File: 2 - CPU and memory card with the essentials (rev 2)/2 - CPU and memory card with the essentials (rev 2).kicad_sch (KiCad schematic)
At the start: 7 parts, among them J1 BUS 1, U1 74HC74, X1 20 MHz, X2 3.6864 MHz

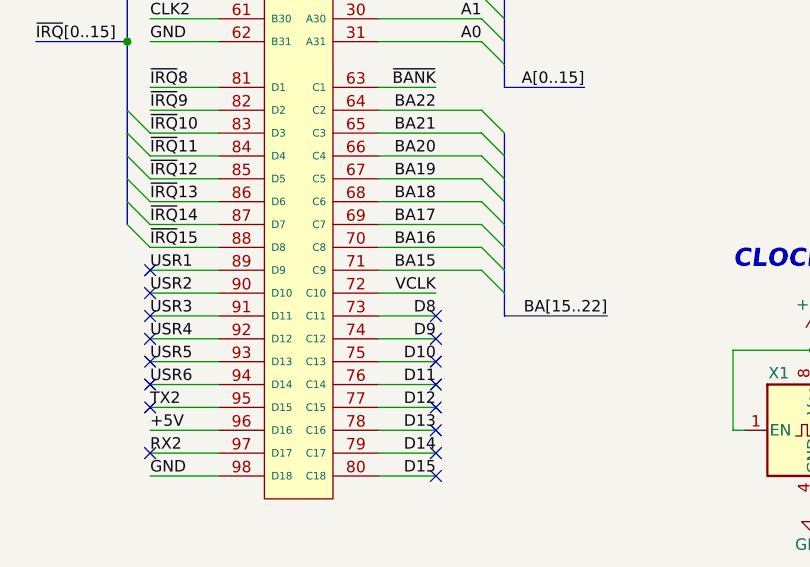
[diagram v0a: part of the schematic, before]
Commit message: Minor tweaks to the backplane, and will be sending it out for manufacture
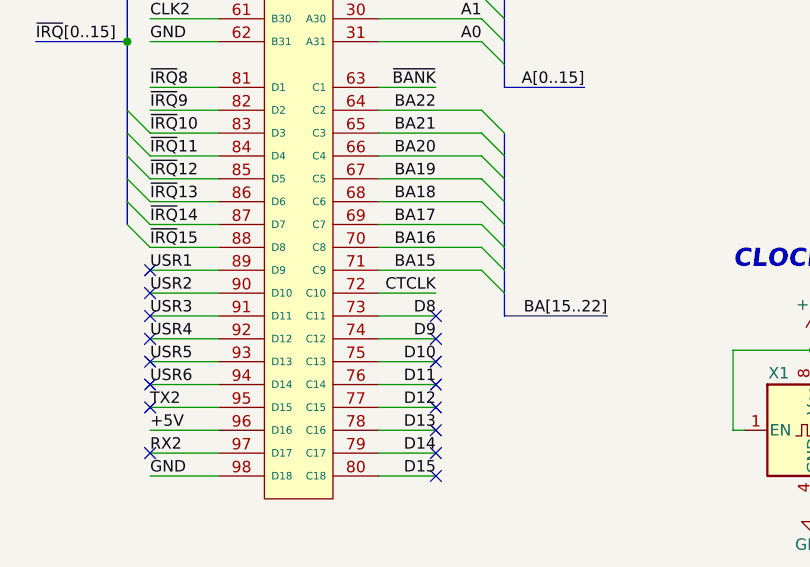
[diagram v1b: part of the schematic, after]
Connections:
- net VCLK: no longer J1.72 (C10)
- new net CTCLK: J1.72 (C10)
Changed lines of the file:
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@@
     (effects (font (size 1.27 1.27)) (justify left bottom))
   )
-  (label "VCLK" (at 59.69 129.54 180) (fields_autoplaced)
+  (label "CTCLK" (at 59.69 129.54 180) (fields_autoplaced)
     (effects (font (size 1.27 1.27)) (justify right bottom))
   )

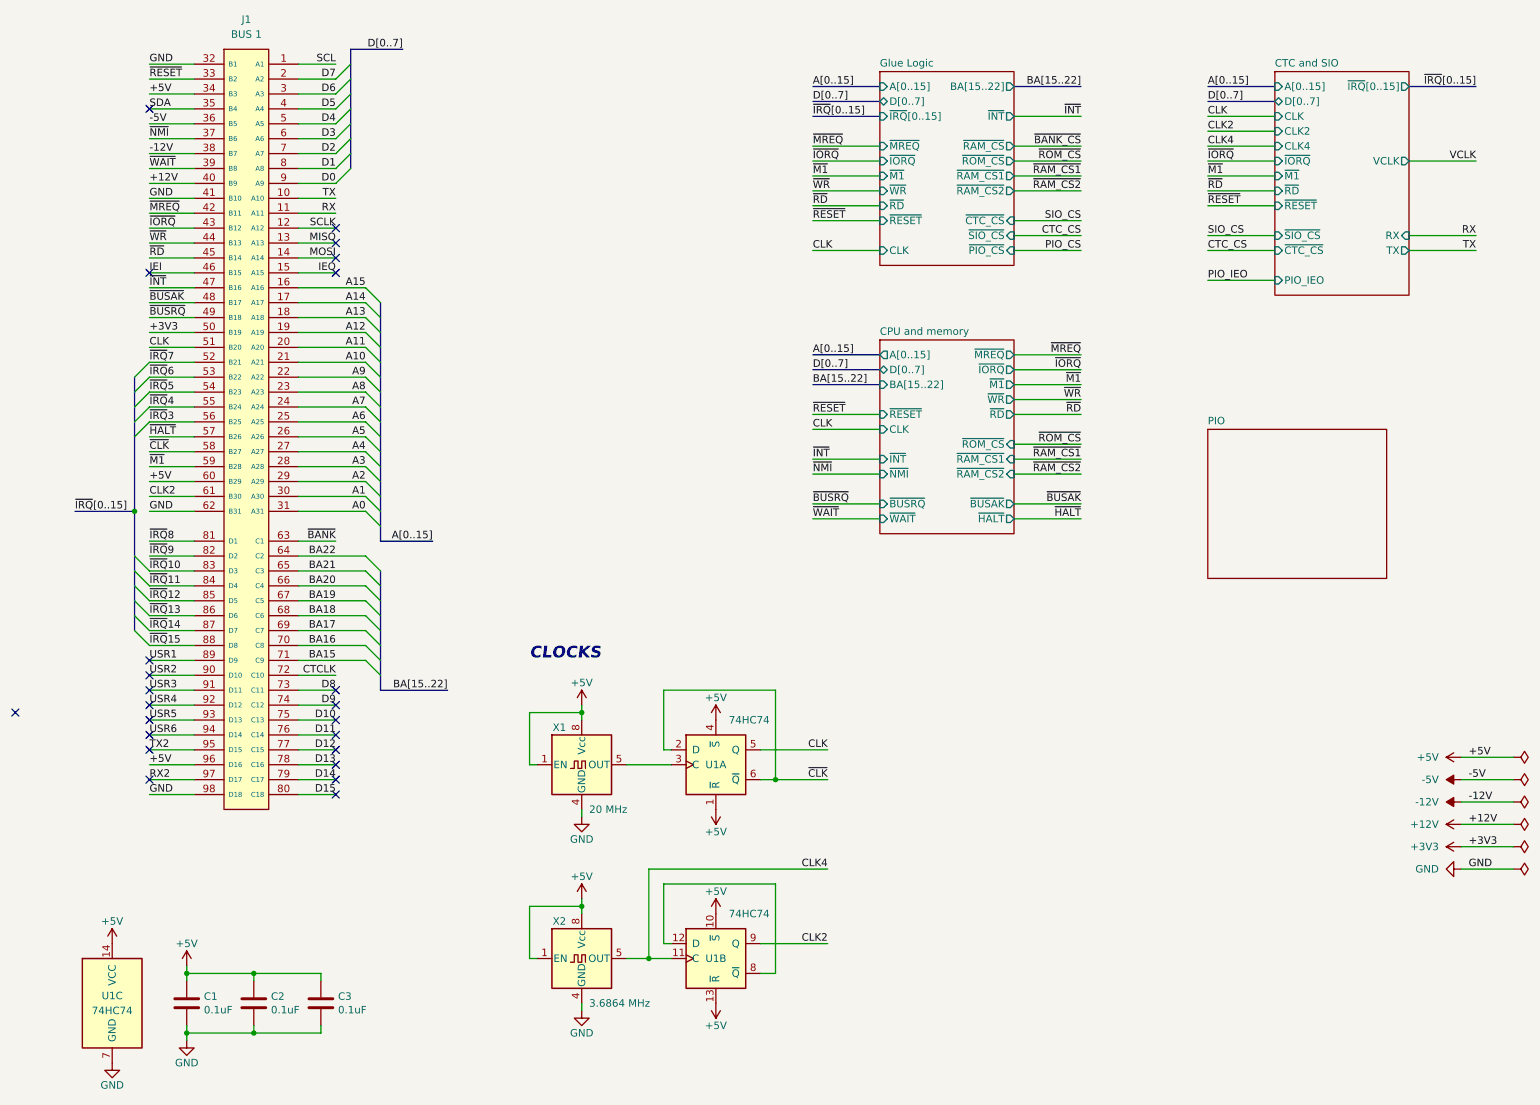
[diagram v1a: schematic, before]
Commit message: Updated disk activity circuit in mother board, and improved layout in CPU card
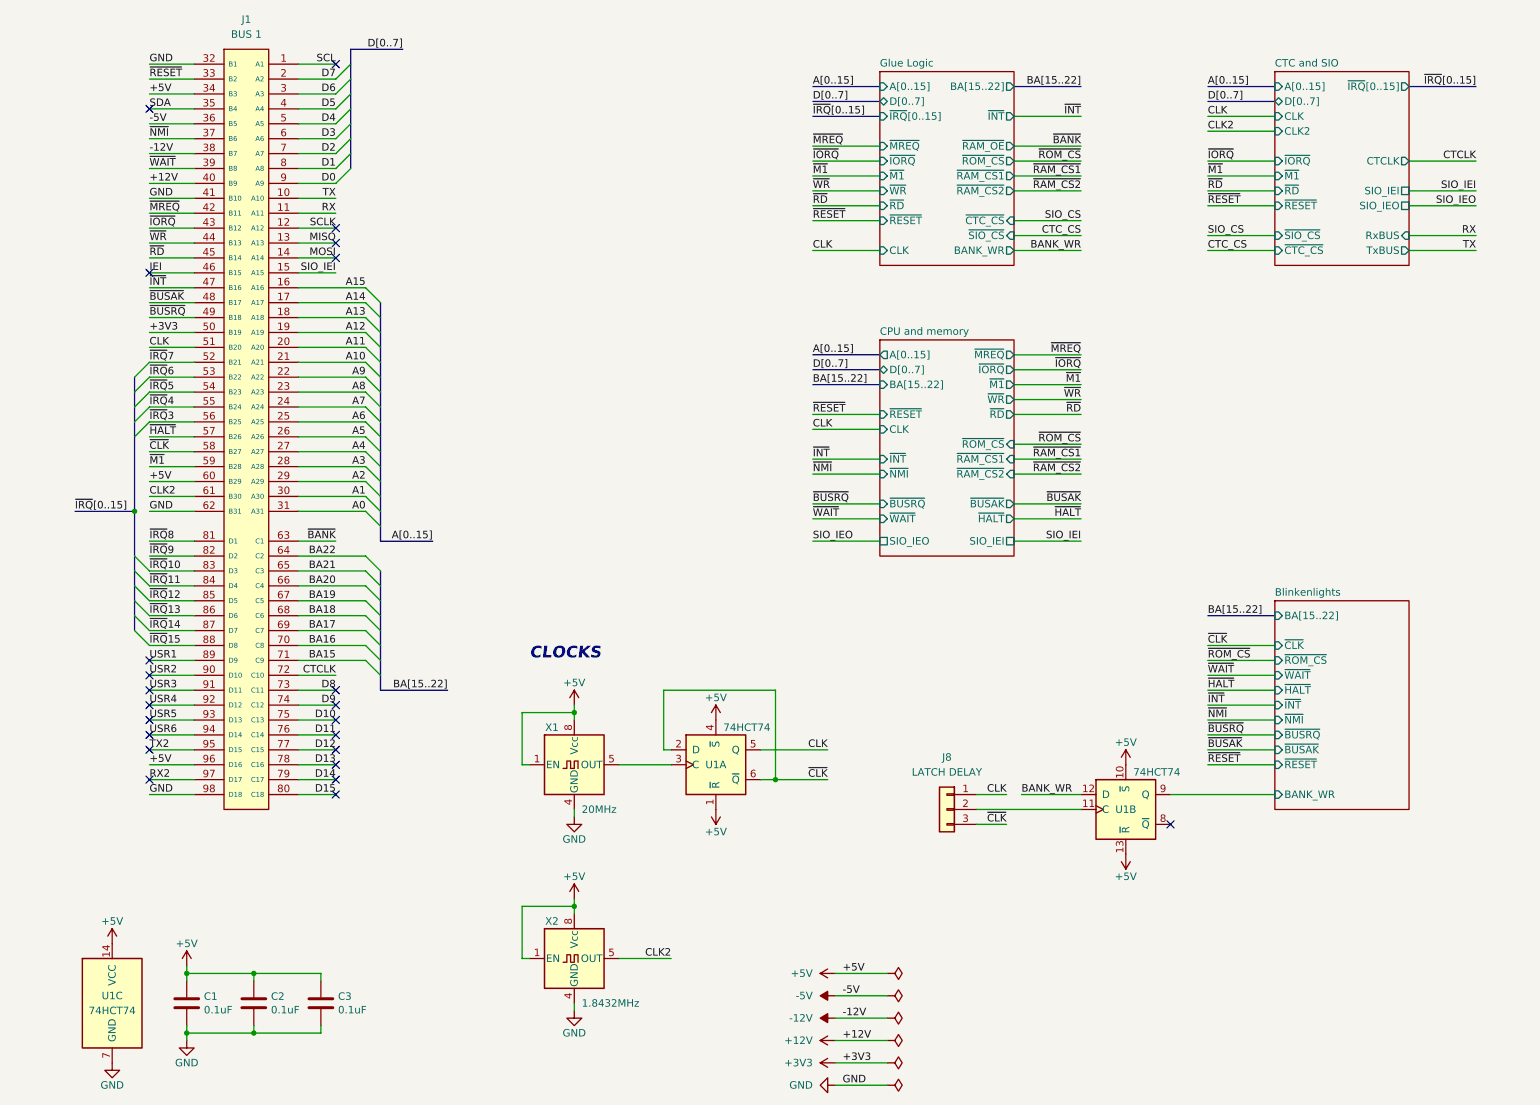
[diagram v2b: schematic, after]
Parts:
- added J8: LATCH DELAY, Connector_PinHeader_2.54mm:PinHeader_1x03_P2.54mm_Vertical, symbol Connector_Generic:Conn_01x03
- U1: value 74HC74 -> 74HCT74
- X1: value 20 MHz -> 20MHz
- X2: value 3.6864 MHz -> 1.8432MHz
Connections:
- net CLK: now also J8.1 (Pin_1)
- net CLK2: now also X2.5 (OUT); no longer U1.9 (Q)
- net ~{CLK}: now also J8.3 (Pin_3)
- net at U1.8 (~{Q}): no longer U1.12 (D)
- net CLK4: no longer names the net of U1.11 (C)
- net CLK4: now also J8.2 (Pin_2); no longer X2.5 (OUT)
- net IEO renamed SIO_IEI
- new net BANK_WR: U1.12 (D)
- new net Blinkenlights/BANK_WR: U1.9 (Q)
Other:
- removed sheet PIO
- added sheet Blinkenlights (Blinkenlights.kicad_sch)
- sheet CPU and memory ports: added SIO_IEI, SIO_IEO; removed none
- sheet CTC and SIO ports: added CTCLK, RxBUS, SIO_IEI, SIO_IEO, TxBUS; removed CLK4, PIO_IEO, RX, TX, VCLK
- sheet Glue Logic ports: added BANK_WR, ~{RAM_OE}; removed ~{PIO_CS}, ~{RAM_CS}
- moved on the sheet: X1, X2

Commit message: Trying to hash out the flaws
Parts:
- removed J1: BUS 1, 0_Library:BUS_AT v2, symbol 0_Library:ISA_CARD_CONNECTOR_16BIT
- removed J8: LATCH DELAY, Connector_PinHeader_2.54mm:PinHeader_1x03_P2.54mm_Vertical, symbol Connector_Generic:Conn_01x03
- removed unit 2 of U1
- removed unit 1 of U1
- added J1: ISA, 0_Library:BUS_XT v2, symbol 0_Library:ISA_CARD_CONNECTOR_8BIT
- X1: value 20MHz -> 10MHz
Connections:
- net +12V: now also J1.40 (B9)
- net +3V3: now also J1.50 (B19)
- net +5V: now also J1.34 (B3), J1.60 (B29)
- net -12V: now also J1.38 (B7)
- net -5V: now also J1.36 (B5)
- net A0: now also J1.31 (A31)
- net A1: now also J1.30 (A30)
- net A10: now also J1.21 (A21)
- net A11: now also J1.20 (A20)
- net A12: now also J1.19 (A19)
- net A13: now also J1.18 (A18)
- net A14: now also J1.17 (A17)
- net A15: now also J1.16 (A16)
- net A2: now also J1.29 (A29)
- net A3: now also J1.28 (A28)
- net A4: now also J1.27 (A27)
- net A5: now also J1.26 (A26)
- net A6: now also J1.25 (A25)
- net A7: now also J1.24 (A24)
- net A8: now also J1.23 (A23)
- net A9: now also J1.22 (A22)
- net CLK: now also X1.5 (OUT), J1.51 (B20)
- net CLK2: now also J1.61 (B30)
- net D0: now also J1.9 (A9)
- net D1: now also J1.8 (A8)
- net D2: now also J1.7 (A7)
- net D3: now also J1.6 (A6)
- net D4: now also J1.5 (A5)
- net D5: now also J1.4 (A4)
- net D6: now also J1.3 (A3)
- net D7: now also J1.2 (A2)
- net GND: now also J1.32 (B1), J1.41 (B10), J1.62 (B31)
- net IEI: now also J1.46 (B15)
- net MISO: now also J1.13 (A13)
- net MOSI: now also J1.14 (A14)
- net RX: now also J1.11 (A11)
- net SCL: now also J1.1 (A1)
- net SCLK: now also J1.12 (A12)
- net SDA: now also J1.35 (B4)
- net SIO_IEI: now also J1.15 (A15)
- net TX: now also J1.10 (A10)
- net ~{BUSAK}: now also J1.48 (B17)
- net ~{BUSRQ}: now also J1.49 (B18)
- net ~{CLK}: now also J1.58 (B27)
- net ~{HALT}: now also J1.57 (B26)
- net ~{INT}: now also J1.47 (B16)
- net ~{IORQ}: now also J1.43 (B12)
- net ~{IRQ}3: now also J1.56 (B25)
- net ~{IRQ}4: now also J1.55 (B24)
- net ~{IRQ}5: now also J1.54 (B23)
- net ~{IRQ}6: now also J1.53 (B22)
- net ~{IRQ}7: now also J1.52 (B21)
- net ~{M1}: now also J1.59 (B28)
- net ~{MREQ}: now also J1.42 (B11)
- net ~{NMI}: now also J1.37 (B6)
- net ~{RD}: now also J1.45 (B14)
- net ~{RESET}: now also J1.33 (B2)
- net ~{WAIT}: now also J1.39 (B8)
- net ~{WR}: now also J1.44 (B13)
- no-connect marks 23 -> 6
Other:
- sheet Blinkenlights ports: added none; removed BANK_WR, BA[15..22]
